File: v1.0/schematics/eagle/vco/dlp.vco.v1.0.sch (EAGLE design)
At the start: 101 parts, among them IC1 NTE912P, IC2 TL074P, IC3 4013N, IC4 TL074P, IC5 TL074P, IC7 TL074P, J1 PWM, J10 SW OUT, J2 LIN FM, J3 SQ OUT, J4 EXP FM, J5 PITCH, J6 SW OUT, J7 SUB OUT, J8 OSC1 OUT, J9 EXP FM, Q1 2N3417, Q2 2N3417, Q3 2N3906, Q4 2N3417, Q5 2N3417, Q6 2N3906

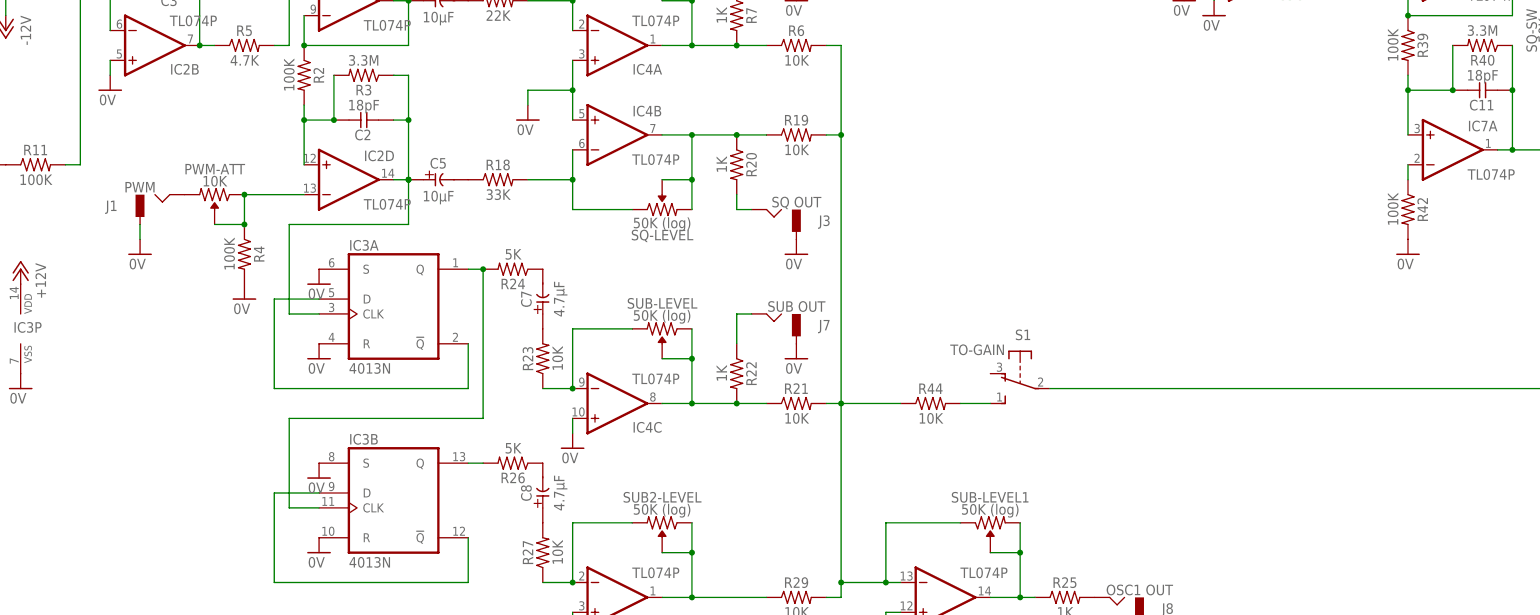
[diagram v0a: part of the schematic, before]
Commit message: Changed PWM on OSC1. Added PWM Knob to OSC2 Updated resistor value on OSC1 SQ wave.
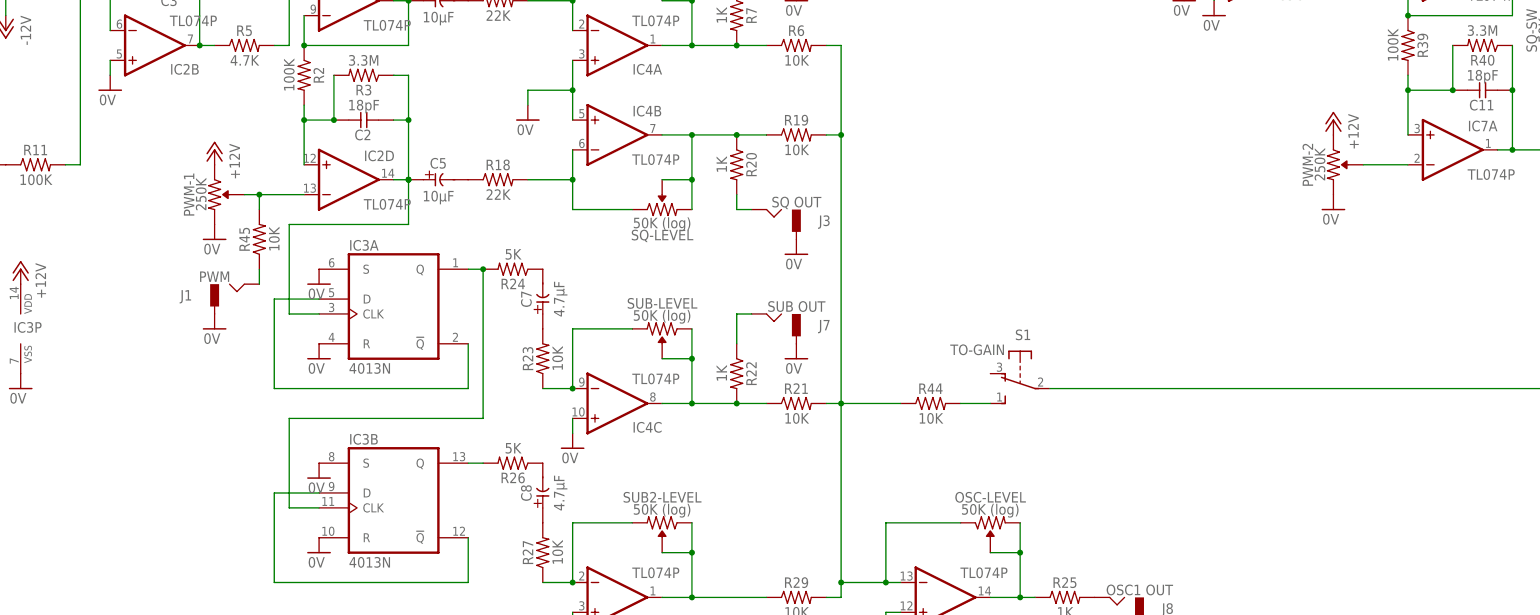
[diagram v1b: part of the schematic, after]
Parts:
- removed R4, R42: 100K, _common:R0309/10
- added PWM-2: 250K, _common:R-VAR
- added R45: 10K, _common:R0309/10
- PWM-1: value 10K -> 250K
- R18: value 33K -> 22K
- renumbered PWM-ATT to PWM-1, SUB-LEVEL1 to OSC-LEVEL
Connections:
- removed net N$71: IC7A.-IN, R42.1
- new net N$46: IC7A.-IN, PWM-2.P$1
- net +12V: now also PWM-1.1, PWM-2.1
- net 0V: now also PWM-1.2, PWM-2.2; no longer R4.2, R42.2
- net N$10: now also IC2D.-IN, PWM-1.P$1, R45.2; no longer J1.HOT, PWM-1.2
- net N$8: now also J1.HOT, R45.1; no longer IC2D.-IN, PWM-1.1, PWM-1.P$1, R4.1
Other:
- moved on the sheet: J1
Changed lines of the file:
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@@
 <setting verticaltext="up"/>
 </settings>
-<grid distance="0.1" unitdist="inch" unit="inch" style="lines" multiple="1" display="yes" altdistance="0.01" altunitdist="inch" altunit="inch"/>
+<grid distance="0.1" unitdist="inch" unit="inch" style="lines" multiple="1" display="no" altdistance="0.01" altunitdist="inch" altunit="inch"/>
 <layers>
 <layer number="1" name="Top" color="4" fill="1" visible="no" active="no"/>
@@
 <part name="R3" library="_common" deviceset="R" device="0309/10" value="3.3M"/>
 <part name="J1" library="_common" deviceset="JACK-M" device="" value="PWM"/>
-<part name="PWM-ATT" library="_common" deviceset="R-VAR" device="" value="10K"/>
-<part name="R4" library="_common" deviceset="R" device="0309/10" value="100K"/>
-<part name="GND5" library="supply1" deviceset="0V" device=""/>
+<part name="PWM-1" library="_common" deviceset="R-VAR" device="" value="250K"/>
 <part name="R5" library="_common" deviceset="R" device="0309/10" value="4.7K"/>
 <part name="C3" library="_common" deviceset="CC-US" device="025-024X044" value="100pF"/>
@@
 <part name="C6" library="_common" deviceset="CE-US" device="E2-5" value="10μF"/>
 <part name="R17" library="_common" deviceset="R" device="0309/10" value="22K"/>
-<part name="R18" library="_common" deviceset="R" device="0309/10" value="33K"/>
+<part name="R18" library="_common" deviceset="R" device="0309/10" value="22K"/>
 <part name="IC4" library="_common" deviceset="TL074" device="P"/>
 <part name="P+6" library="supply1" deviceset="+12V" device=""/>
@@
 <part name="GND18" library="supply1" deviceset="0V" device=""/>
 <part name="GND19" library="supply1" deviceset="0V" device=""/>
-<part name="SUB-LEVEL1" library="_common" deviceset="R-VAR" device="" value="50K (log)"/>
+<part name="OSC-LEVEL" library="_common" deviceset="R-VAR" device="" value="50K (log)"/>
 <part name="R25" library="_common" deviceset="R" device="0309/10" value="1K"/>
 <part name="J8" library="_common" deviceset="JACK-M" device="" value="OSC1 OUT"/>
@@
 <part name="C12" library="_common" deviceset="CE-US" device="E2-5" value="10μF"/>
 <part name="R41" library="_common" deviceset="R" device="0309/10" value="22K"/>
-<part name="R42" library="_common" deviceset="R" device="0309/10" value="100K"/>
-<part name="GND36" library="supply1" deviceset="0V" device=""/>
 <part name="SQ-SW" library="_common" deviceset="R-VAR" device="" value="50K"/>
 <part name="SW-LEVEL1" library="_common" deviceset="R-VAR" device="" value="OSC2-LEVEL"/>
@@
 <part name="P+12" library="supply1" deviceset="+12V" device=""/>
 <part name="P-7" library="supply1" deviceset="-12V" device=""/>
+<part name="P+13" library="supply1" deviceset="+12V" device=""/>
+<part name="GND39" library="supply1" deviceset="0V" device=""/>
+<part name="R45" library="_common" deviceset="R" device="0309/10" value="10K"/>
+<part name="PWM-2" library="_common" deviceset="R-VAR" device="" value="250K"/>
+<part name="P+14" library="supply1" deviceset="+12V" device=""/>
+<part name="GND40" library="supply1" deviceset="0V" device=""/>
 </parts>
 <sheets>
@@
 <instance part="IC2" gate="C" x="30.48" y="25.4"/>
 <instance part="IC2" gate="D" x="30.48" y="-5.08"/>
-<instance part="GND4" gate="1" x="-5.08" y="-17.78"/>
+<instance part="GND4" gate="1" x="7.62" y="-30.48"/>
 <instance part="R2" gate="G$1" x="22.86" y="12.7" rot="R270"/>
 <instance part="C2" gate="G$1" x="33.02" y="5.08" rot="R90"/>
 <instance part="R3" gate="G$1" x="33.02" y="12.7" rot="R180"/>
-<instance part="J1" gate="G$1" x="-2.54" y="-10.16"/>
-<instance part="PWM-ATT" gate="G$1" x="7.62" y="-7.62" rot="R180"/>
-<instance part="R4" gate="G$1" x="12.7" y="-17.78" rot="R270"/>
-<instance part="GND5" gate="1" x="12.7" y="-25.4"/>
+<instance part="J1" gate="G$1" x="10.16" y="-25.4"/>
+<instance part="PWM-1" gate="G$1" x="7.62" y="-7.62" rot="R270"/>
 <instance part="R5" gate="G$1" x="12.7" y="17.78"/>
 <instance part="C3" gate="G$1" x="0" y="27.94" rot="R90"/>
@@
 <instance part="GND18" gate="1" x="68.58" y="-50.8"/>
 <instance part="GND19" gate="1" x="121.92" y="-83.82" rot="MR0"/>
-<instance part="SUB-LEVEL1" gate="G$1" x="139.7" y="-63.5" rot="MR180"/>
+<instance part="OSC-LEVEL" gate="G$1" x="139.7" y="-63.5" rot="MR180"/>
 <instance part="R25" gate="G$1" x="152.4" y="-76.2"/>
 <instance part="J8" gate="G$1" x="162.56" y="-78.74" rot="MR0"/>
@@
 <instance part="C12" gate="G$1" x="246.38" y="20.32" rot="MR270"/>
 <instance part="R41" gate="G$1" x="256.54" y="20.32"/>
-<instance part="R42" gate="G$1" x="210.82" y="-10.16" rot="R270"/>
-<instance part="GND36" gate="1" x="210.82" y="-17.78"/>
 <instance part="SQ-SW" gate="G$1" x="236.22" y="20.32" rot="R270"/>
 <instance part="SW-LEVEL1" gate="G$1" x="274.32" y="30.48" rot="R180"/>
@@
 <instance part="IC1" gate="C" x="193.04" y="81.28" rot="MR90"/>
 <instance part="IC1" gate="D" x="218.44" y="81.28" rot="R90"/>
+<instance part="P+13" gate="1" x="7.62" y="0" rot="MR0"/>
+<instance part="GND39" gate="1" x="7.62" y="-15.24"/>
+<instance part="R45" gate="G$1" x="15.24" y="-15.24" rot="R90"/>
+<instance part="PWM-2" gate="G$1" x="198.12" y="-2.54" rot="R270"/>
+<instance part="P+14" gate="1" x="198.12" y="5.08" rot="MR0"/>
+<instance part="GND40" gate="1" x="198.12" y="-10.16"/>
 </instances>
 <busses>
@@
 </segment>
 <segment>
-<pinref part="R4" gate="G$1" pin="2"/>
-<pinref part="GND5" gate="1" pin="0V"/>
-</segment>
-<segment>
 <pinref part="J1" gate="G$1" pin="GND"/>
 <pinref part="GND4" gate="1" pin="0V"/>
-<wire x1="-5.08" y1="-15.24" x2="-5.08" y2="-12.7" width="0.1524" layer="91"/>
 </segment>
 <segment>
@@
 </segment>
 <segment>
-<pinref part="R42" gate="G$1" pin="2"/>
-<pinref part="GND36" gate="1" pin="0V"/>
-</segment>
-<segment>
 <pinref part="IC7" gate="B" pin="+IN"/>
 <pinref part="GND37" gate="1" pin="0V"/>
@@
 <pinref part="J10" gate="G$1" pin="GND"/>
 <pinref part="GND38" gate="1" pin="0V"/>
+</segment>
+<segment>
+<pinref part="PWM-1" gate="G$1" pin="2"/>
+<pinref part="GND39" gate="1" pin="0V"/>
+</segment>
+<segment>
+<pinref part="PWM-2" gate="G$1" pin="2"/>
+<pinref part="GND40" gate="1" pin="0V"/>
 </segment>
 </net>
@@
 <pinref part="IC7" gate="P" pin="V+"/>
 <pinref part="P+12" gate="1" pin="+12V"/>
+</segment>
+<segment>
+<pinref part="PWM-1" gate="G$1" pin="1"/>
+<pinref part="P+13" gate="1" pin="+12V"/>
+</segment>
+<segment>
+<pinref part="PWM-2" gate="G$1" pin="1"/>
+<pinref part="P+14" gate="1" pin="+12V"/>
 </segment>
 </net>
@@
 </segment>
 </net>
-<net name="N$8" class="0">
-<segment>
-<pinref part="PWM-ATT" gate="G$1" pin="P$1"/>
-<pinref part="R4" gate="G$1" pin="1"/>
-<wire x1="7.62" y1="-12.7" x2="12.7" y2="-12.7" width="0.1524" layer="91"/>
-<pinref part="IC2" gate="D" pin="-IN"/>
-<wire x1="12.7" y1="-12.7" x2="12.7" y2="-7.62" width="0.1524" layer="91"/>
-<junction x="12.7" y="-12.7"/>
-<pinref part="PWM-ATT" gate="G$1" pin="1"/>
-<junction x="12.7" y="-7.62"/>
-<wire x1="12.7" y1="-7.62" x2="22.86" y2="-7.62" width="0.1524" layer="91"/>
-</segment>
-</net>
-<net name="N$10" class="0">
-<segment>
-<pinref part="PWM-ATT" gate="G$1" pin="2"/>
-<pinref part="J1" gate="G$1" pin="HOT"/>
-</segment>
-</net>
 <net name="N$11" class="0">
 <segment>
@@
 <segment>
 <pinref part="IC4" gate="D" pin="OUT"/>
-<pinref part="SUB-LEVEL1" gate="G$1" pin="P$1"/>
+<pinref part="OSC-LEVEL" gate="G$1" pin="P$1"/>
 <wire x1="139.7" y1="-68.58" x2="144.78" y2="-68.58" width="0.1524" layer="91"/>
-<pinref part="SUB-LEVEL1" gate="G$1" pin="2"/>
+<pinref part="OSC-LEVEL" gate="G$1" pin="2"/>
 <wire x1="144.78" y1="-63.5" x2="144.78" y2="-68.58" width="0.1524" layer="91"/>
 <pinref part="R25" gate="G$1" pin="1"/>
@@
 <junction x="228.6" y="10.16"/>
 <junction x="228.6" y="0"/>
-</segment>
-</net>
-<net name="N$71" class="0">
-<segment>
-<pinref part="IC7" gate="A" pin="-IN"/>
-<pinref part="R42" gate="G$1" pin="1"/>
-<wire x1="210.82" y1="-2.54" x2="210.82" y2="-5.08" width="0.1524" layer="91"/>
 </segment>
 </net>
@@
 <wire x1="114.3" y1="-76.2" x2="114.3" y2="-73.66" width="0.1524" layer="91"/>
 <pinref part="IC4" gate="D" pin="-IN"/>
-<pinref part="SUB-LEVEL1" gate="G$1" pin="1"/>
+<pinref part="OSC-LEVEL" gate="G$1" pin="1"/>
 <wire x1="121.92" y1="-63.5" x2="134.62" y2="-63.5" width="0.1524" layer="91"/>
 <wire x1="121.92" y1="-63.5" x2="121.92" y2="-73.66" width="0.1524" layer="91"/>
@@
 </segment>
 </net>
+<net name="N$8" class="0">
+<segment>
+<pinref part="J1" gate="G$1" pin="HOT"/>
+<pinref part="R45" gate="G$1" pin="1"/>
+<wire x1="15.24" y1="-22.86" x2="15.24" y2="-20.32" width="0.1524" layer="91"/>
+</segment>
+</net>
+<net name="N$10" class="0">
+<segment>
+<pinref part="PWM-1" gate="G$1" pin="P$1"/>
+<pinref part="IC2" gate="D" pin="-IN"/>
+<wire x1="12.7" y1="-7.62" x2="15.24" y2="-7.62" width="0.1524" layer="91"/>
+<pinref part="R45" gate="G$1" pin="2"/>
+<wire x1="15.24" y1="-7.62" x2="22.86" y2="-7.62" width="0.1524" layer="91"/>
+<wire x1="15.24" y1="-10.16" x2="15.24" y2="-7.62" width="0.1524" layer="91"/>
+<junction x="15.24" y="-7.62"/>
+</segment>
+</net>
+<net name="N$46" class="0">
+<segment>
+<pinref part="PWM-2" gate="G$1" pin="P$1"/>
+<pinref part="IC7" gate="A" pin="-IN"/>
+<wire x1="203.2" y1="-2.54" x2="210.82" y2="-2.54" width="0.1524" layer="91"/>
+</segment>
+</net>

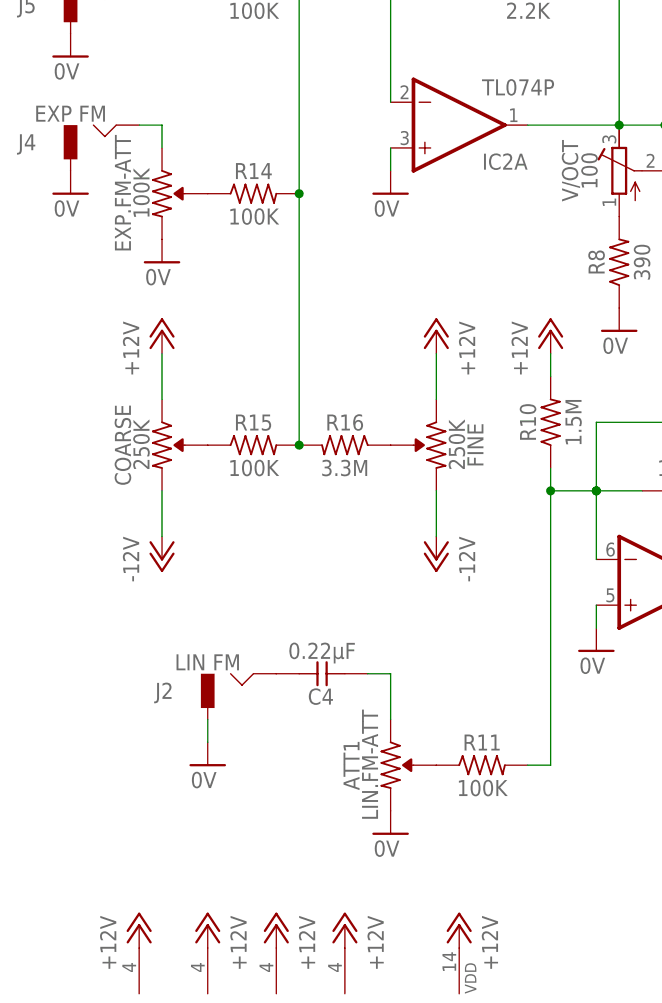
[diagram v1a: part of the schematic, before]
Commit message: Updated vco with correct pot values Updated vcf with new values and added in manual CV control.
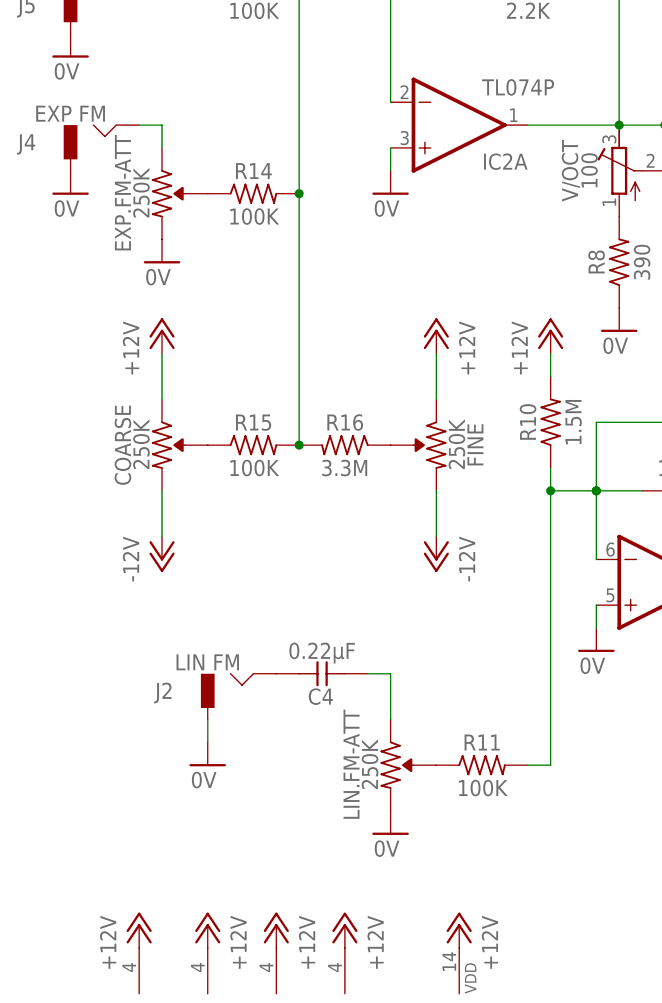
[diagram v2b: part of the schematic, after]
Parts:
- EXP.FM-ATT: value 100K -> 250K
- LIN.FM-ATT: value LIN.FM-ATT -> 250K
- renumbered ATT1 to LIN.FM-ATT
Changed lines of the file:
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@@
 <?xml version="1.0" encoding="utf-8"?>
 <!DOCTYPE eagle SYSTEM "eagle.dtd">
-<eagle version="6.1">
+<eagle version="6.5.0">
 <drawing>
 <settings>
@@
 <part name="P+2" library="supply1" deviceset="+12V" device=""/>
 <part name="R11" library="_common" deviceset="R" device="0309/10" value="100K"/>
-<part name="ATT1" library="_common" deviceset="R-VAR" device="" value="LIN.FM-ATT"/>
+<part name="LIN.FM-ATT" library="_common" deviceset="R-VAR" device="" value="250K"/>
 <part name="C4" library="_common" deviceset="CC-US" device="025-024X044" value="0.22μF"/>
 <part name="J2" library="_common" deviceset="JACK-M" device="" value="LIN FM"/>
@@
 <part name="FINE" library="_common" deviceset="R-VAR" device="" value="250K"/>
 <part name="COARSE" library="_common" deviceset="R-VAR" device="" value="250K"/>
-<part name="EXP.FM-ATT" library="_common" deviceset="R-VAR" device="" value="100K"/>
+<part name="EXP.FM-ATT" library="_common" deviceset="R-VAR" device="" value="250K"/>
 <part name="J4" library="_common" deviceset="JACK-M" device="" value="EXP FM"/>
 <part name="J5" library="_common" deviceset="JACK-M" device="" value="PITCH"/>
@@
 <instance part="P+2" gate="1" x="-15.24" y="45.72"/>
 <instance part="R11" gate="G$1" x="-22.86" y="-2.54"/>
-<instance part="ATT1" gate="G$1" x="-33.02" y="-2.54" rot="R270"/>
+<instance part="LIN.FM-ATT" gate="G$1" x="-33.02" y="-2.54" rot="R270"/>
 <instance part="C4" gate="G$1" x="-40.64" y="7.62" rot="R90"/>
 <instance part="J2" gate="G$1" x="-50.8" y="5.08"/>
@@
 </segment>
 <segment>
-<pinref part="ATT1" gate="G$1" pin="2"/>
+<pinref part="LIN.FM-ATT" gate="G$1" pin="2"/>
 <pinref part="GND9" gate="1" pin="0V"/>
 </segment>
@@
 <segment>
 <pinref part="R11" gate="G$1" pin="1"/>
-<pinref part="ATT1" gate="G$1" pin="P$1"/>
+<pinref part="LIN.FM-ATT" gate="G$1" pin="P$1"/>
 </segment>
 </net>
 <net name="N$19" class="0">
 <segment>
-<pinref part="ATT1" gate="G$1" pin="1"/>
+<pinref part="LIN.FM-ATT" gate="G$1" pin="1"/>
 <pinref part="C4" gate="G$1" pin="2"/>
 <wire x1="-35.56" y1="7.62" x2="-33.02" y2="7.62" width="0.1524" layer="91"/>
